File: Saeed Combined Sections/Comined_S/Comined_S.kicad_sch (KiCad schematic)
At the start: 34 parts, among them Q1 SI2301CDS-T1-GE3, SW1 JS202011SCQN, U1 DRV8833PW, U2 DRV8833PW, U3 INA219AxDCN, U4 AMS1117-3.3, U5 TPS63802DLAR

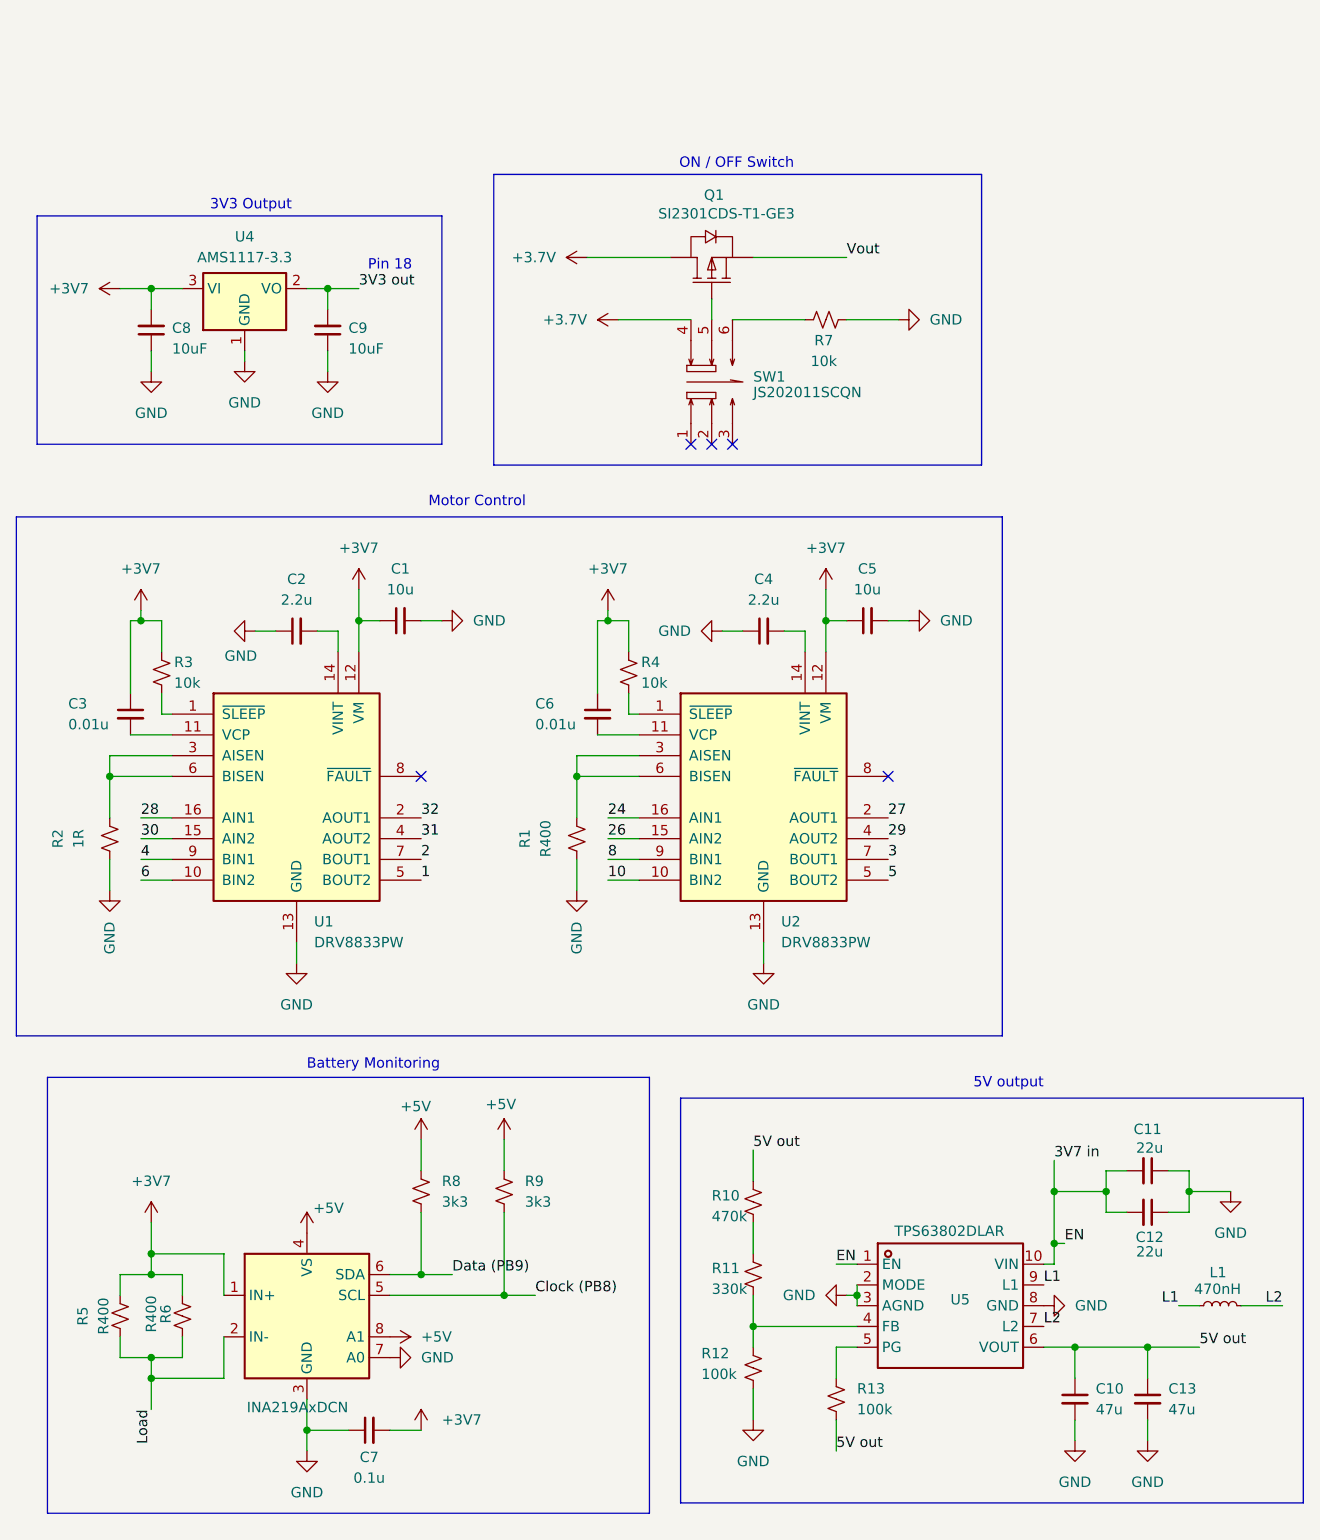
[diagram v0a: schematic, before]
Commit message: Changed switch
Changed switch do not depend on p-mosfet
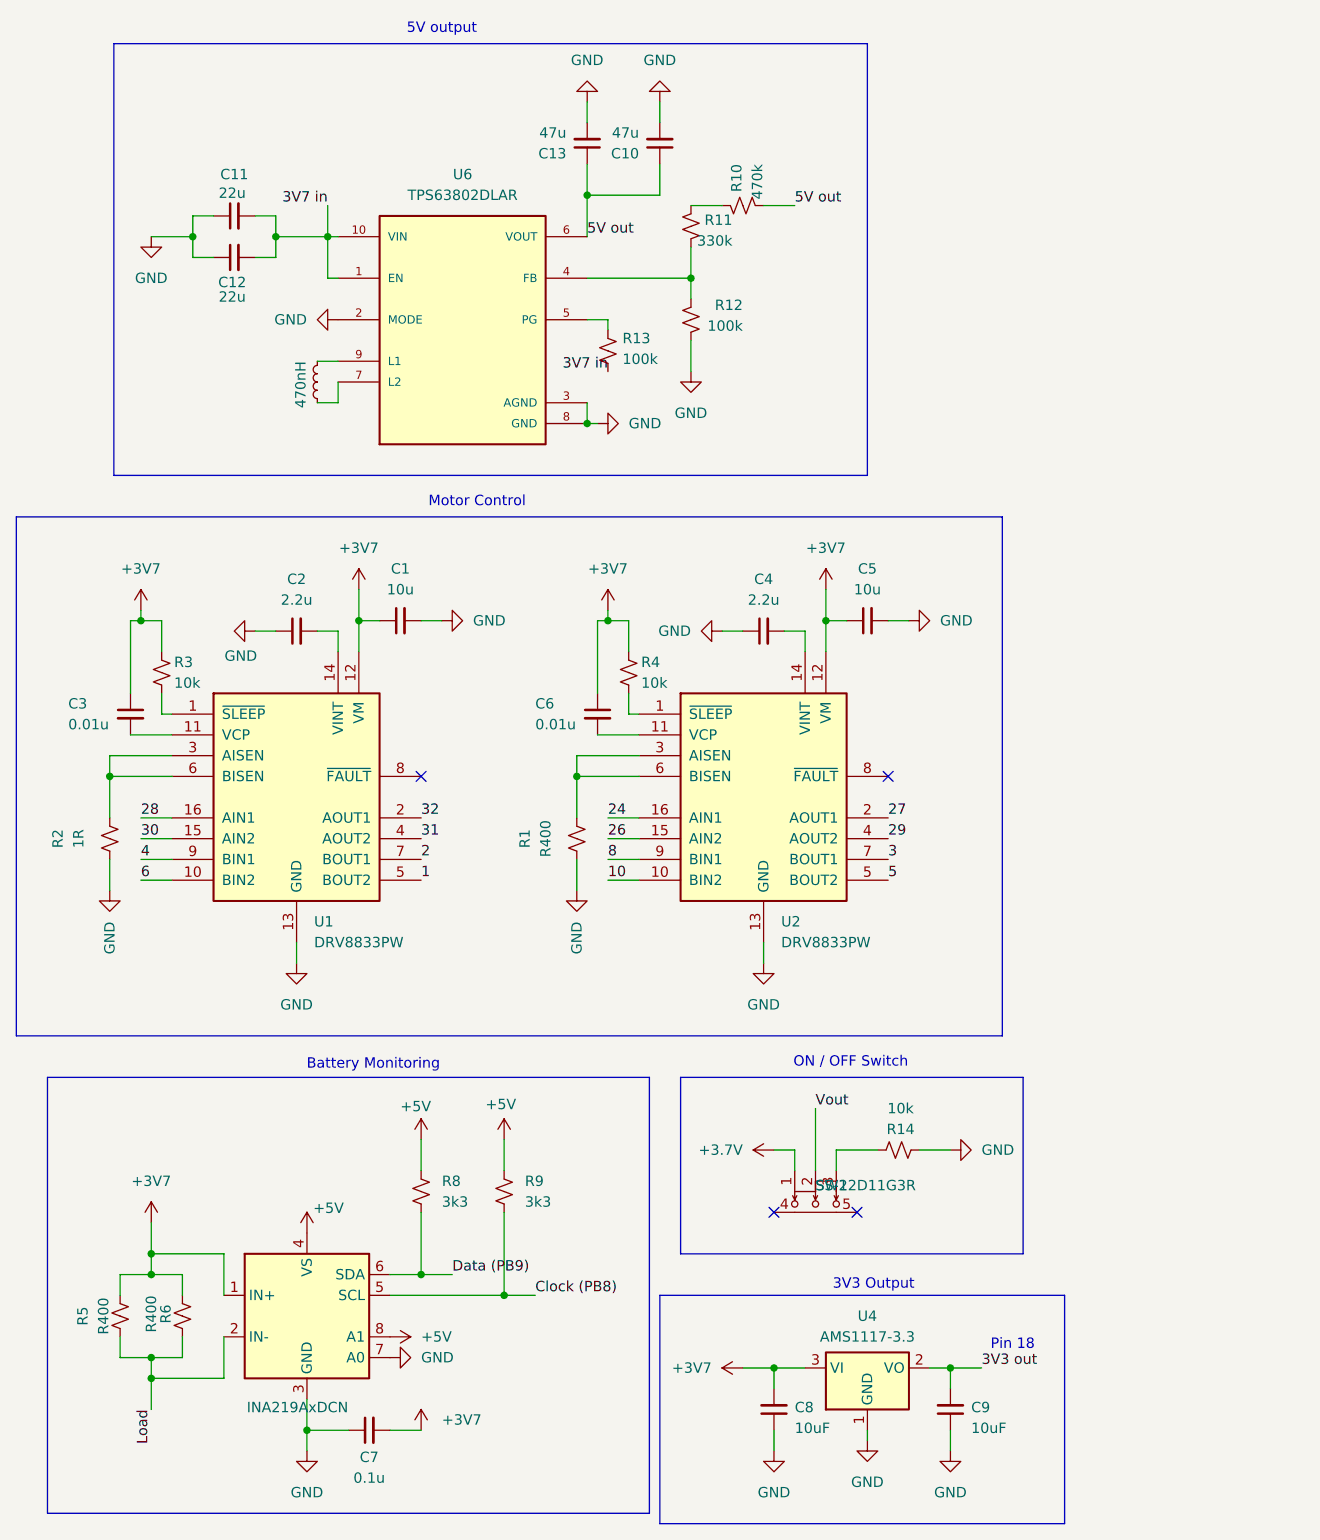
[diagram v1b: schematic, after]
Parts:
- removed Q1: SI2301CDS-T1-GE3, Package_TO_SOT_SMD:SOT-23_Handsoldering, symbol temp-altium-import:root_0_SI2301CDS-T1-GE3_
- removed R7: 10k, Resistor_SMD:R_0402_1005Metric_Pad0.72x0.64mm_HandSolder, symbol Device:R_Small_US
- removed SW1: JS202011SCQN, Button_Switch_THT:SW_CK_JS202011AQN_DPDT_Angled, symbol ON_OFF_Switch-altium-import:root_0_JS202011SCQN_
- removed U5: TPS63802DLAR, VSON-10_L3.0-W2.0-P0.50-TL, symbol temp-altium-import:root_0_TPS63802DLAR_C2845237
- added R14: 10k, Resistor_SMD:R_0402_1005Metric_Pad0.72x0.64mm_HandSolder, symbol Device:R_Small_US
- added SW2: SS-12D11G3R, SS-12D11G3R:SW-TH_SS-12D11L3, symbol temp-altium-import:root_0_SS-12D11G3R_
- added U6: TPS63802DLAR, TPS63802DLAR:VREG_TPS63802DLAR, symbol TPS63802DLAR:TPS63802DLAR
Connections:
- net +3.7V: now also SW2.1
- net 3V7 in: now also R13.2, U6.1 (EN), U6.10 (VIN)
- net 5V out: now also R10.2, U6.6 (VOUT); no longer R10.1, R13.2
- net GND: now also R14.1, U6.2 (MODE), U6.3 (AGND), U6.8 (GND)
- net Vout: now also SW2.2
- net at R11.2, R12.1: now also U6.4 (FB)
- net at R11.1: now also R10.1; no longer R10.2
- net at R13.1: now also U6.5 (PG)
- net L1: no longer names the net of L1.1
- net L1: now also U6.7 (L2)
- net L2: no longer names the net of L1.2
- net L2: now also U6.9 (L1)
- new net: R14.2, SW2.3
- no-connect marks 5 -> 4
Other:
- moved on the sheet: C10, C11, C12, C13, C8, C9, R10, R11, R12, R13, U4
